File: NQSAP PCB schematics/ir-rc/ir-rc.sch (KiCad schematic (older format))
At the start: 9 parts, among them J1 Bus, J2 Bus, J3 Conn_02x08, J4 Conn_02x08, J5 Conn_02x08, J6 Conn_02x08

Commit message: Add Microcode and IR/RC modules.  Add clock circuit to Loader module.
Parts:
- removed J5, J6: Conn_02x08, Connector_PinHeader_2.54mm:PinHeader_2x08_P2.54mm_Vertical, symbol Connector_Generic:Conn_02x08_Top_Bottom
- added C4, C5: 0.1uF, Capacitor_SMD:C_0805_2012Metric_Pad1.18x1.45mm_HandSolder, symbol Device:C
- added D1: IR0, LED_SMD:LED_0805_2012Metric_Pad1.15x1.40mm_HandSolder, symbol Device:LED_Small
- added D10: T0, LED_SMD:LED_0805_2012Metric_Pad1.15x1.40mm_HandSolder, symbol Device:LED_Small
- added D11: T1, LED_SMD:LED_0805_2012Metric_Pad1.15x1.40mm_HandSolder, symbol Device:LED_Small
- added D12: T2, LED_SMD:LED_0805_2012Metric_Pad1.15x1.40mm_HandSolder, symbol Device:LED_Small
- added D13: T3, LED_SMD:LED_0805_2012Metric_Pad1.15x1.40mm_HandSolder, symbol Device:LED_Small
- added D14: T4, LED_SMD:LED_0805_2012Metric_Pad1.15x1.40mm_HandSolder, symbol Device:LED_Small
- added D15: T5, LED_SMD:LED_0805_2012Metric_Pad1.15x1.40mm_HandSolder, symbol Device:LED_Small
- added D16: T6, LED_SMD:LED_0805_2012Metric_Pad1.15x1.40mm_HandSolder, symbol Device:LED_Small
- added D17: T7, LED_SMD:LED_0805_2012Metric_Pad1.15x1.40mm_HandSolder, symbol Device:LED_Small
- added D18: WRITE, LED_SMD:LED_0805_2012Metric_Pad1.15x1.40mm_HandSolder, symbol Device:LED_Small
- added D2: IR1, LED_SMD:LED_0805_2012Metric_Pad1.15x1.40mm_HandSolder, symbol Device:LED_Small
- added D3: IR2, LED_SMD:LED_0805_2012Metric_Pad1.15x1.40mm_HandSolder, symbol Device:LED_Small
- added D4: IR3, LED_SMD:LED_0805_2012Metric_Pad1.15x1.40mm_HandSolder, symbol Device:LED_Small
- added D5: IR4, LED_SMD:LED_0805_2012Metric_Pad1.15x1.40mm_HandSolder, symbol Device:LED_Small
- added D6: IR5, LED_SMD:LED_0805_2012Metric_Pad1.15x1.40mm_HandSolder, symbol Device:LED_Small
- added D7: IR6, LED_SMD:LED_0805_2012Metric_Pad1.15x1.40mm_HandSolder, symbol Device:LED_Small
- added D8: IR7, LED_SMD:LED_0805_2012Metric_Pad1.15x1.40mm_HandSolder, symbol Device:LED_Small
- added D9: T-EXT, LED_SMD:LED_0805_2012Metric_Pad1.15x1.40mm_HandSolder, symbol Device:LED_Small
- added R1, R2, R3, R4, R5, R6, R7, R8: R-GRN, Resistor_SMD:R_0805_2012Metric_Pad1.20x1.40mm_HandSolder, symbol Device:R_Small_US
- added R10, R11, R12, R13, R14, R15, R16, R17: R-YEL, Resistor_SMD:R_0805_2012Metric_Pad1.20x1.40mm_HandSolder, symbol Device:R_Small_US
- added R18: R-RED, Resistor_SMD:R_0805_2012Metric_Pad1.20x1.40mm_HandSolder, symbol Device:R_Small_US
- added R9: R-WHT, Resistor_SMD:R_0805_2012Metric_Pad1.20x1.40mm_HandSolder, symbol Device:R_Small_US
- added U1, U2: 74HCT377, Package_DIP:DIP-20_W7.62mm, symbol 74xx:74LS377
- added U3: 74HCT161, Package_DIP:DIP-16_W7.62mm, symbol 74xx:74LS161
- added U4, U5: 74HCT138, Package_DIP:DIP-16_W7.62mm, symbol 74xx:74LS138
- C1, C2, C3: footprint (none) -> Capacitor_SMD:C_0805_2012Metric_Pad1.18x1.45mm_HandSolder
- J3, J4: footprint Connector_PinHeader_2.54mm:PinHeader_2x08_P2.54mm_Vertical -> Connector_PinHeader_2.54mm:PinHeader_1x08_P2.54mm_Vertical; symbol Connector_Generic:Conn_02x08_Top_Bottom -> Connector_Generic:Conn_01x08
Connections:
- net labels added: MA0, MA1, MA10, MA11, MA2, MA3, MA4, MA5, MA6, MA7, MA8, MA9, VCC, ~CLK, ~RST, ~WI
- net labels removed: +5V, C0, C1, CC, CS, FB, FC, FN, FV, FZ, JE, LDR-ACT, LDR-CLK, LF, NC-1, NC-2, PI, RR0, RR1, RR2, RR3, RST, SE, SI, XX0
- wire segments 98 -> 304
- no-connect marks 0 -> 72
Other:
- note added: "INSTRUCTION\nREGISTER"
- note added: "IR BUFFERED\n"
- note added: "RING COUNTER"
- moved on the sheet: C1, C2, C3, J1, J2

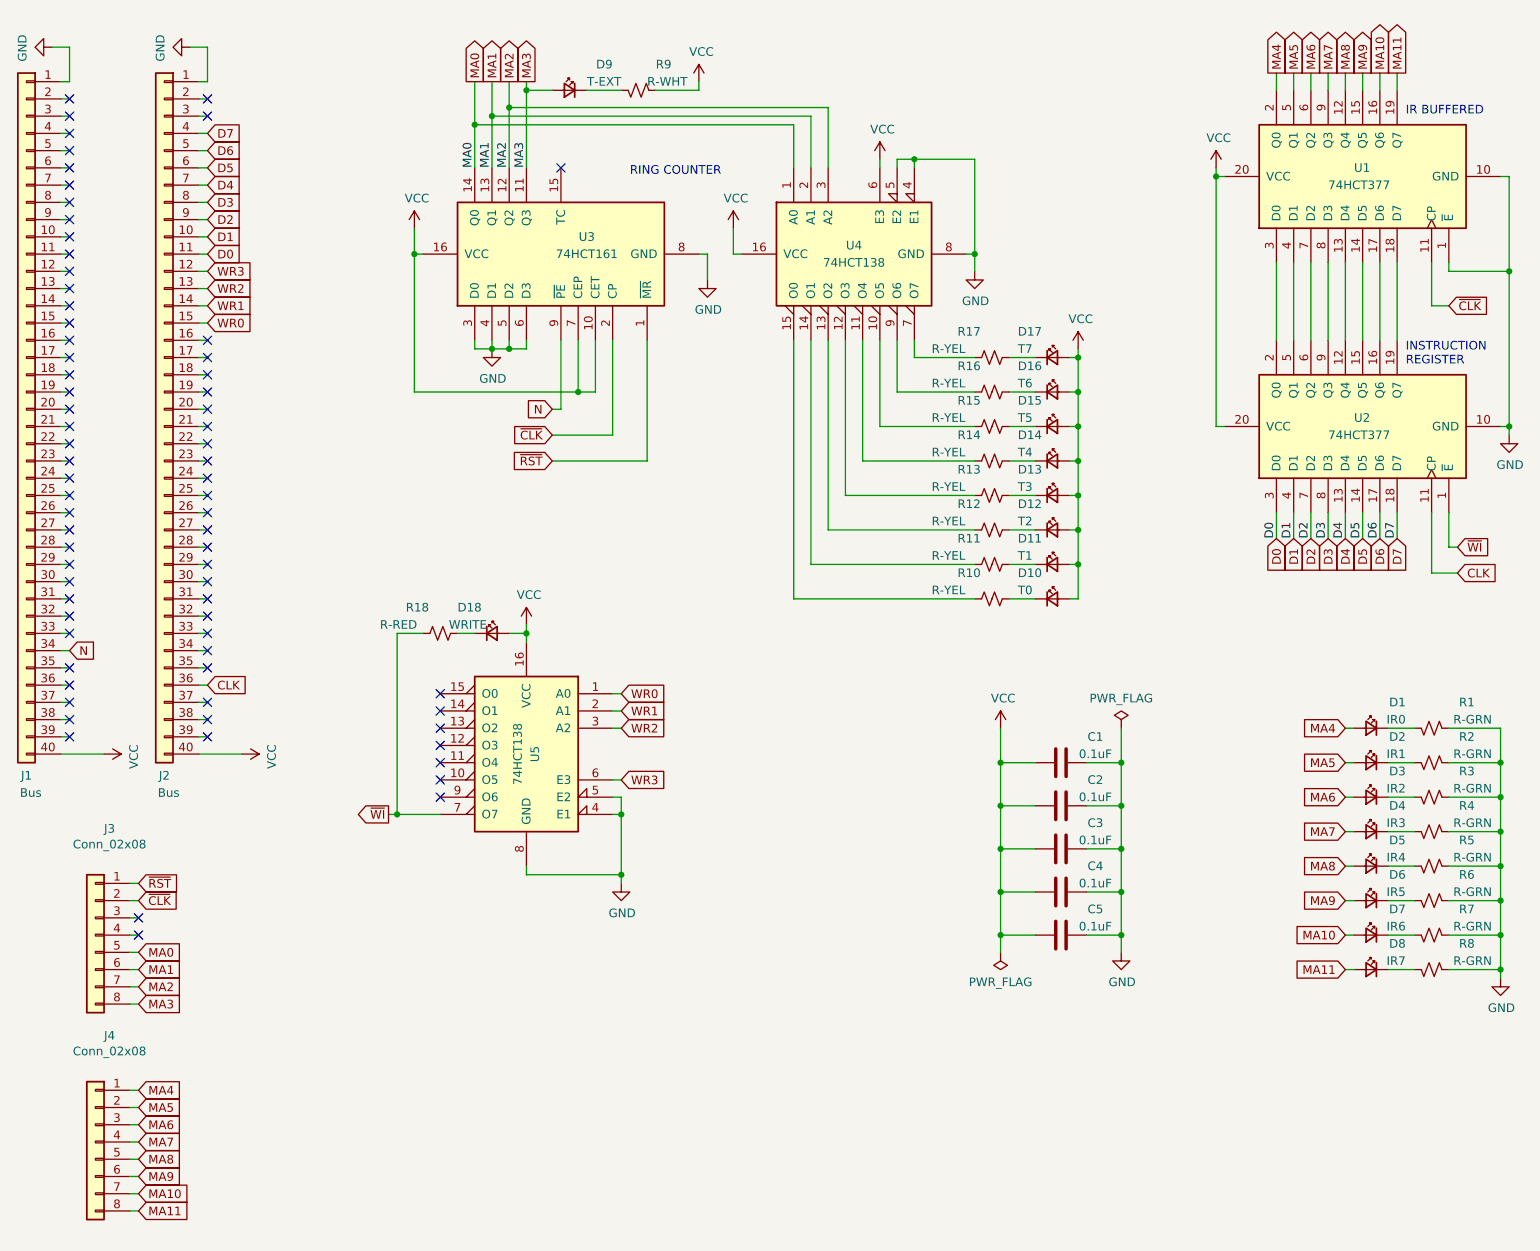
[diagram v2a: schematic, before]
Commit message: updated KiCads and gerbers for the AB Registers and IR/RC module
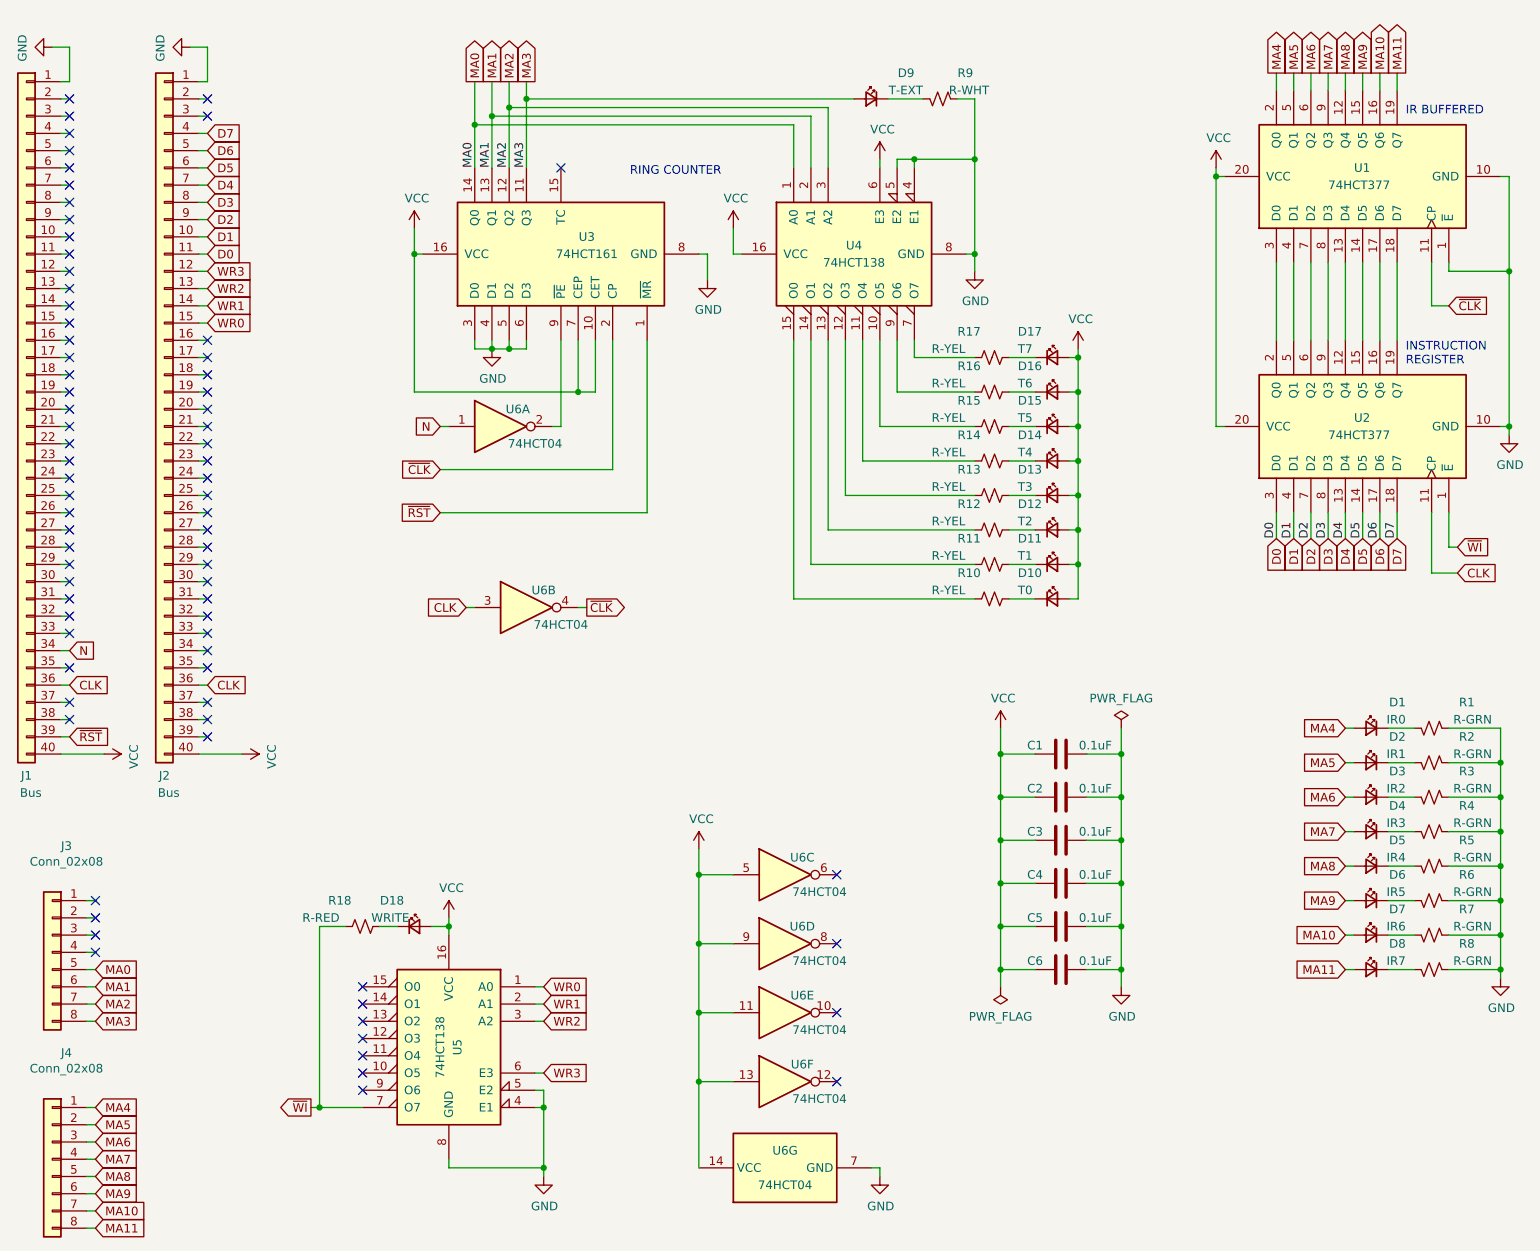
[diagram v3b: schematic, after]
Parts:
- added C6: 0.1uF, Capacitor_SMD:C_0805_2012Metric_Pad1.18x1.45mm_HandSolder, symbol Device:C
- added U6: 74HCT04, Package_DIP:DIP-14_W7.62mm, symbol 74xx:74HCT04
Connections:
- net CLK: now also J1.36 (Pin_36), U6.3
- net GND: now also R9.1, C6.1, U6.7 (GND)
- net N: now also U6.1; no longer U3.9 (~PE)
- net VCC: now also C6.2, U6.11, U6.13, U6.14 (VCC), U6.5, U6.9; no longer R9.1
- net ~CLK: now also U6.4; no longer J3.2 (Pin_2)
- net ~RST: now also J1.39 (Pin_39); no longer J3.1 (Pin_1)
- new net: U3.9 (~PE), U6.2
- no-connect marks 72 -> 76
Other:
- moved on the sheet: C1, C2, C3, C4, C5, D18, D9, J3, J4, R18, R9, U5
